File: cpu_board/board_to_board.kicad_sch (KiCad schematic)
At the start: 2 parts

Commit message: grounded
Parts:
- J? (x2): footprint adcs:HIROSE_DF40C-100DP-0.4V(51) -> adcs:DF40C100DP04V51
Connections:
- net GPIO_DISP_B2_00: no longer J?.50
- net GPIO_DISP_B2_01: no longer J?.52
- net GPIO_DISP_B2_02: no longer J?.54
- net GPIO_DISP_B2_03: no longer J?.56
- net GPIO_DISP_B2_04: no longer J?.60
- net GPIO_DISP_B2_05: no longer J?.62
- net GPIO_DISP_B2_06: no longer J?.64
- net GPIO_DISP_B2_07: no longer J?.66
- net GPIO_DISP_B2_08: no longer J?.70
- net GPIO_DISP_B2_09: no longer J?.72
- net GPIO_DISP_B2_10: no longer J?.74
- net GPIO_DISP_B2_11: no longer J?.76
- net GPIO_DISP_B2_12: no longer J?.80
- net GPIO_DISP_B2_13: no longer J?.82
- net GPIO_DISP_B2_14: no longer J?.84
- net GPIO_DISP_B2_15: no longer J?.86
- new net GPIO_EMC_B1_40: J?.50
- new net GPIO_EMC_B1_41: J?.52
- no-connect marks 0 -> 14
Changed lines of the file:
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@@
   (junction (at 99.06 107.95) (diameter 0) (color 0 0 0 0)
   )
+  (no_connect (at 129.54 151.13))
+  (no_connect (at 129.54 166.37))
+  (no_connect (at 129.54 171.45))
+  (no_connect (at 129.54 184.15))
+  (no_connect (at 129.54 186.69))
+  (no_connect (at 129.54 176.53))
+  (no_connect (at 129.54 158.75))
+  (no_connect (at 129.54 153.67))
+  (no_connect (at 129.54 173.99))
+  (no_connect (at 129.54 191.77))
+  (no_connect (at 129.54 189.23))
+  (no_connect (at 129.54 163.83))
+  (no_connect (at 129.54 179.07))
+  (no_connect (at 129.54 161.29))
   (wire (pts (xy 307.975 186.055) (xy 310.515 186.055))
     (stroke (width 0) (type default))
@@
     )
   )
-  (global_label "GPIO_DISP_B2_02" (shape bidirectional) (at 129.54 151.13 0) (fields_autoplaced)
-    (effects (font (size 1.27 1.27)) (justify left))
-    (property "Intersheetrefs" "${INTERSHEET_REFS}" (at 147.3043 151.13 0)
-      (effects (font (size 1.27 1.27)) (justify left) hide)
-    )
-  )
   (global_label "GPIO_AD_10" (shape bidirectional) (at 96.52 148.59 180) (fields_autoplaced)
     (effects (font (size 1.27 1.27)) (justify right))
@@
     )
   )
-  (global_label "GPIO_DISP_B2_12" (shape bidirectional) (at 129.54 184.15 0) (fields_autoplaced)
-    (effects (font (size 1.27 1.27)) (justify left))
-    (property "Intersheetrefs" "${INTERSHEET_REFS}" (at 147.3043 184.15 0)
-      (effects (font (size 1.27 1.27)) (justify left) hide)
-    )
-  )
-  (global_label "GPIO_DISP_B2_15" (shape bidirectional) (at 129.54 191.77 0) (fields_autoplaced)
-    (effects (font (size 1.27 1.27)) (justify left))
-    (property "Intersheetrefs" "${INTERSHEET_REFS}" (at 147.3043 191.77 0)
-      (effects (font (size 1.27 1.27)) (justify left) hide)
-    )
-  )
   (global_label "GPIO_SD_B1_03" (shape bidirectional) (at 129.54 118.11 0) (fields_autoplaced)
     (effects (font (size 1.27 1.27)) (justify left))
@@
     )
   )
+  (global_label "GPIO_EMC_B1_41" (shape input) (at 129.54 148.59 0)
+    (effects (font (size 1.27 1.27)) (justify left))
+    (property "Intersheetrefs" "${INTERSHEET_REFS}" (at 129.54 148.59 0)
+      (effects (font (size 1.27 1.27)) hide)
+    )
+  )
   (global_label "GPIO_EMC_B2_08" (shape bidirectional) (at 278.765 155.575 180)
     (effects (font (size 1.27 1.27)) (justify right))
@@
     )
   )
-  (global_label "GPIO_DISP_B2_00" (shape bidirectional) (at 129.54 146.05 0) (fields_autoplaced)
-    (effects (font (size 1.27 1.27)) (justify left))
-    (property "Intersheetrefs" "${INTERSHEET_REFS}" (at 148.0448 146.05 0)
-      (effects (font (size 1.27 1.27)) (justify left) hide)
-    )
-  )
   (global_label "GPIO_AD_28" (shape bidirectional) (at 96.52 201.93 180) (fields_autoplaced)
     (effects (font (size 1.27 1.27)) (justify right))
@@
     )
   )
-  (global_label "GPIO_DISP_B2_05" (shape bidirectional) (at 129.54 161.29 0) (fields_autoplaced)
-    (effects (font (size 1.27 1.27)) (justify left))
-    (property "Intersheetrefs" "${INTERSHEET_REFS}" (at 147.3043 161.29 0)
-      (effects (font (size 1.27 1.27)) (justify left) hide)
-    )
-  )
   (global_label "GPIO_AD_15" (shape bidirectional) (at 96.52 163.83 180) (fields_autoplaced)
     (effects (font (size 1.27 1.27)) (justify right))
@@
     )
   )
-  (global_label "GPIO_DISP_B2_03" (shape bidirectional) (at 129.54 153.67 0) (fields_autoplaced)
-    (effects (font (size 1.27 1.27)) (justify left))
-    (property "Intersheetrefs" "${INTERSHEET_REFS}" (at 147.3043 153.67 0)
-      (effects (font (size 1.27 1.27)) (justify left) hide)
-    )
-  )
   (global_label "MIPI_CSI_D0_P" (shape input) (at 313.055 188.595 0) (fields_autoplaced)
     (effects (font (size 1.27 1.27)) (justify left))
@@
     )
   )
-  (global_label "GPIO_DISP_B2_09" (shape bidirectional) (at 129.54 173.99 0) (fields_autoplaced)
-    (effects (font (size 1.27 1.27)) (justify left))
-    (property "Intersheetrefs" "${INTERSHEET_REFS}" (at 147.3043 173.99 0)
-      (effects (font (size 1.27 1.27)) (justify left) hide)
-    )
-  )
-  (global_label "GPIO_DISP_B2_08" (shape bidirectional) (at 129.54 171.45 0) (fields_autoplaced)
-    (effects (font (size 1.27 1.27)) (justify left))
-    (property "Intersheetrefs" "${INTERSHEET_REFS}" (at 147.3043 171.45 0)
-      (effects (font (size 1.27 1.27)) (justify left) hide)
-    )
-  )
   (global_label "GPIO_AD_01" (shape bidirectional) (at 96.52 118.11 180) (fields_autoplaced)
     (effects (font (size 1.27 1.27)) (justify right))
@@
     )
   )
-  (global_label "GPIO_DISP_B2_13" (shape bidirectional) (at 129.54 186.69 0) (fields_autoplaced)
-    (effects (font (size 1.27 1.27)) (justify left))
-    (property "Intersheetrefs" "${INTERSHEET_REFS}" (at 147.3043 186.69 0)
-      (effects (font (size 1.27 1.27)) (justify left) hide)
-    )
-  )
-  (global_label "GPIO_DISP_B2_11" (shape bidirectional) (at 129.54 179.07 0) (fields_autoplaced)
-    (effects (font (size 1.27 1.27)) (justify left))
-    (property "Intersheetrefs" "${INTERSHEET_REFS}" (at 147.3043 179.07 0)
-      (effects (font (size 1.27 1.27)) (justify left) hide)
-    )
-  )
   (global_label "USDHC2_DATA2" (shape bidirectional) (at 129.54 130.81 0) (fields_autoplaced)
     (effects (font (size 1.27 1.27)) (justify left))
@@
     )
   )
-  (global_label "GPIO_DISP_B2_06" (shape bidirectional) (at 129.54 163.83 0) (fields_autoplaced)
-    (effects (font (size 1.27 1.27)) (justify left))
-    (property "Intersheetrefs" "${INTERSHEET_REFS}" (at 147.3043 163.83 0)
-      (effects (font (size 1.27 1.27)) (justify left) hide)
+  (global_label "GPIO_EMC_B1_40" (shape output) (at 129.54 146.05 0)
+    (effects (font (size 1.27 1.27)) (justify left))
+    (property "Intersheetrefs" "${INTERSHEET_REFS}" (at 129.54 146.05 0)
+      (effects (font (size 1.27 1.27)) hide)
     )
   )
@@
     )
   )
-  (global_label "GPIO_DISP_B2_10" (shape bidirectional) (at 129.54 176.53 0) (fields_autoplaced)
-    (effects (font (size 1.27 1.27)) (justify left))
-    (property "Intersheetrefs" "${INTERSHEET_REFS}" (at 147.3043 176.53 0)
-      (effects (font (size 1.27 1.27)) (justify left) hide)
-    )
-  )
   (global_label "GPIO_DISP_B2_11" (shape bidirectional) (at 313.055 173.355 0) (fields_autoplaced)
     (effects (font (size 1.27 1.27)) (justify left))
@@
     )
   )
-  (global_label "GPIO_DISP_B2_07" (shape bidirectional) (at 129.54 166.37 0) (fields_autoplaced)
-    (effects (font (size 1.27 1.27)) (justify left))
-    (property "Intersheetrefs" "${INTERSHEET_REFS}" (at 147.3043 166.37 0)
-      (effects (font (size 1.27 1.27)) (justify left) hide)
-    )
-  )
   (global_label "GPIO_LPSR_07" (shape bidirectional) (at 96.52 105.41 180) (fields_autoplaced)
     (effects (font (size 1.27 1.27)) (justify right))
@@
     )
   )
-  (global_label "GPIO_DISP_B2_01" (shape bidirectional) (at 129.54 148.59 0) (fields_autoplaced)
-    (effects (font (size 1.27 1.27)) (justify left))
-    (property "Intersheetrefs" "${INTERSHEET_REFS}" (at 147.3043 148.59 0)
-      (effects (font (size 1.27 1.27)) (justify left) hide)
-    )
-  )
   (global_label "GPIO_DISP_B1_05" (shape bidirectional) (at 313.055 117.475 0) (fields_autoplaced)
     (effects (font (size 1.27 1.27)) (justify left))
@@
     )
   )
-  (global_label "GPIO_DISP_B2_14" (shape bidirectional) (at 129.54 189.23 0) (fields_autoplaced)
-    (effects (font (size 1.27 1.27)) (justify left))
-    (property "Intersheetrefs" "${INTERSHEET_REFS}" (at 147.3043 189.23 0)
-      (effects (font (size 1.27 1.27)) (justify left) hide)
-    )
-  )
   (global_label "GPIO_EMC_B2_00" (shape bidirectional) (at 278.765 132.715 180)
     (effects (font (size 1.27 1.27)) (justify right))
@@
     (effects (font (size 1.27 1.27)) (justify left))
     (property "Intersheetrefs" "${INTERSHEET_REFS}" (at 148.3926 120.65 0)
-      (effects (font (size 1.27 1.27)) (justify left) hide)
-    )
-  )
-  (global_label "GPIO_DISP_B2_04" (shape bidirectional) (at 129.54 158.75 0) (fields_autoplaced)
-    (effects (font (size 1.27 1.27)) (justify left))
-    (property "Intersheetrefs" "${INTERSHEET_REFS}" (at 147.3043 158.75 0)
       (effects (font (size 1.27 1.27)) (justify left) hide)
     )
@@
       (effects (font (size 1.27 1.27)) hide)
     )
-    (property "Footprint" "adcs:HIROSE_DF40C-100DP-0.4V(51)" (at 106.68 80.01 0)
+    (property "Footprint" "adcs:DF40C100DP04V51" (at 106.68 80.01 0)
       (effects (font (size 1.27 1.27)) hide)
     )
@@
     (property "Footprint (for JLCPCB)" "" (at 106.68 80.01 0)
       (effects (font (size 1.27 1.27)) hide)
+    )
+    (property "DigiKey Part Number" "" (at 106.68 80.01 0)
+      (effects (font (size 1.27 1.27)) hide)
+    )
+    (property "Tolerance" "" (at 106.68 80.01 0)
+      (effects (font (size 1.27 1.27)))
+    )
+    (property "Power Rating" "" (at 106.68 80.01 0)
+      (effects (font (size 1.27 1.27)))
     )
     (pin "1")
@@
       (effects (font (size 1.27 1.27)) hide)
     )
-    (property "Footprint" "adcs:HIROSE_DF40C-100DP-0.4V(51)" (at 290.195 76.835 0)
+    (property "Footprint" "adcs:DF40C100DP04V51" (at 290.195 76.835 0)
       (effects (font (size 1.27 1.27)) hide)
     )
@@
       (effects (font (size 1.27 1.27)) hide)
     )
+    (property "DigiKey Part Number" "" (at 290.195 76.835 0)
+      (effects (font (size 1.27 1.27)) hide)
+    )
+    (property "Tolerance" "" (at 290.195 76.835 0)
+      (effects (font (size 1.27 1.27)))
+    )
+    (property "Power Rating" "" (at 290.195 76.835 0)
+      (effects (font (size 1.27 1.27)))
+    )
     (pin "1")

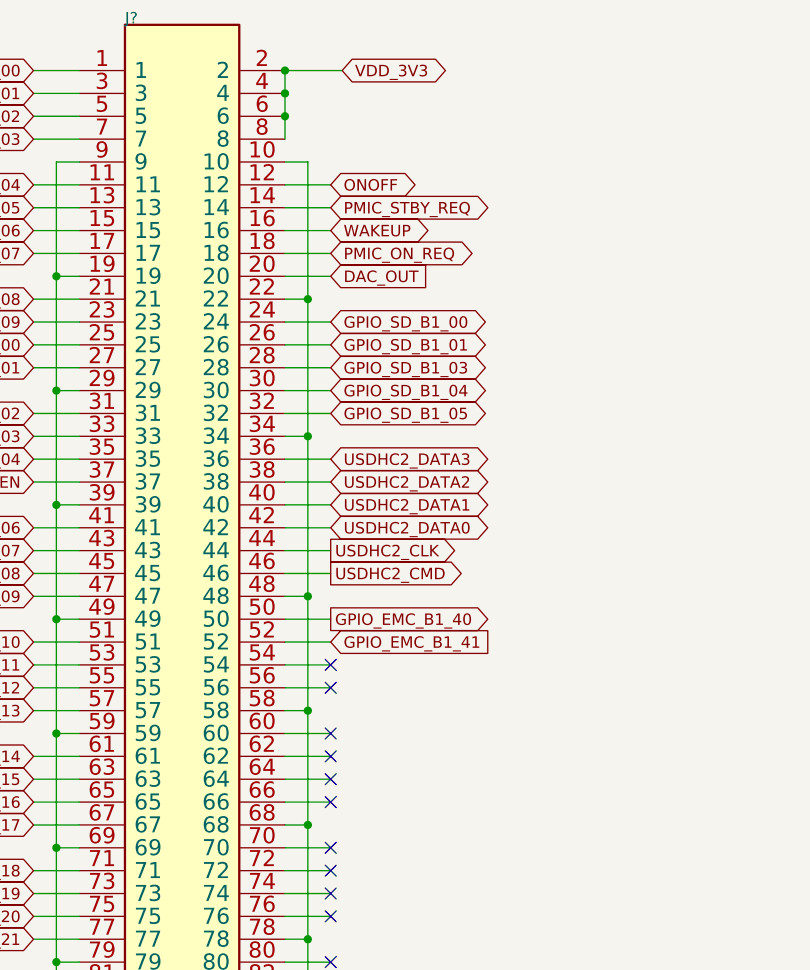
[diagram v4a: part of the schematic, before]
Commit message: add load switch
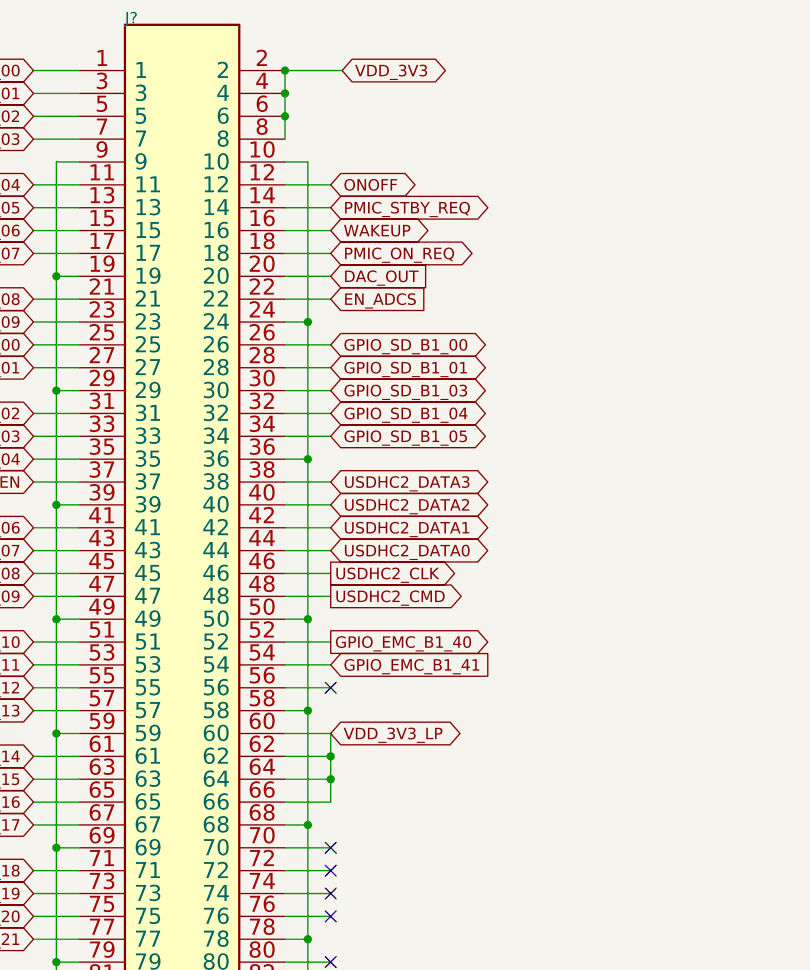
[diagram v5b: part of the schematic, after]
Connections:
- net GND: now also J?.24, J?.36, J?.50; no longer J?.22, J?.34, J?.48
- net GPIO_EMC_B1_40: now also J?.52; no longer J?.50
- net GPIO_EMC_B1_41: now also J?.54; no longer J?.52
- net GPIO_SD_B1_00: now also J?.26; no longer J?.24
- net GPIO_SD_B1_01: now also J?.28; no longer J?.26
- net GPIO_SD_B1_03: now also J?.30; no longer J?.28
- net GPIO_SD_B1_04: now also J?.32; no longer J?.30
- net GPIO_SD_B1_05: now also J?.34; no longer J?.32
- net USDHC2_CLK: now also J?.46; no longer J?.44
- net USDHC2_CMD: now also J?.48; no longer J?.46
- net USDHC2_DATA0: now also J?.44; no longer J?.42
- net USDHC2_DATA1: now also J?.42; no longer J?.40
- net USDHC2_DATA2: now also J?.40; no longer J?.38
- net USDHC2_DATA3: now also J?.38; no longer J?.36
- net VDD_3V3_LP: now reaches J?.60
- net VDD_3V3_LP: now also J?.62, J?.64, J?.66
- new net EN_ADCS: J?.22
- no-connect marks 14 -> 9

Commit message: pre-autorouter
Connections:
- net MIPI_CSI_CK_N: no longer names the net of J?.94
- net MIPI_CSI_CK_P: no longer names the net of J?.92
- net MIPI_CSI_D0_N: no longer names the net of J?.88
- net MIPI_CSI_D0_P: no longer names the net of J?.86
- net MIPI_CSI_D1_N: no longer names the net of J?.100
- net MIPI_CSI_D1_P: no longer names the net of J?.98
- no-connect marks 9 -> 15
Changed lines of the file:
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@@
   )
   (no_connect (at 129.54 171.45))
+  (no_connect (at 313.055 206.375))
   (no_connect (at 129.54 184.15))
   (no_connect (at 129.54 186.69))
+  (no_connect (at 313.055 196.215))
   (no_connect (at 129.54 176.53))
   (no_connect (at 129.54 153.67))
   (no_connect (at 129.54 173.99))
+  (no_connect (at 313.055 198.755))
+  (no_connect (at 313.055 203.835))
   (no_connect (at 129.54 191.77))
+  (no_connect (at 313.055 188.595))
   (no_connect (at 129.54 189.23))
+  (no_connect (at 313.055 191.135))
   (no_connect (at 129.54 179.07))
   (wire (pts (xy 307.975 186.055) (xy 310.515 186.055))
@@
     )
   )
-  (global_label "MIPI_CSI_D0_N" (shape input) (at 313.055 191.135 0) (fields_autoplaced)
-    (effects (font (size 1.27 1.27)) (justify left))
-    (property "Intersheetrefs" "${INTERSHEET_REFS}" (at 329.0995 191.135 0)
-      (effects (font (size 1.27 1.27)) (justify left) hide)
-    )
-  )
-  (global_label "MIPI_CSI_D0_P" (shape input) (at 313.055 188.595 0) (fields_autoplaced)
-    (effects (font (size 1.27 1.27)) (justify left))
-    (property "Intersheetrefs" "${INTERSHEET_REFS}" (at 329.0414 188.595 0)
-      (effects (font (size 1.27 1.27)) (justify left) hide)
-    )
-  )
   (global_label "GPIO_EMC_B2_12" (shape bidirectional) (at 278.765 168.275 180)
     (effects (font (size 1.27 1.27)) (justify right))
@@
     )
   )
-  (global_label "MIPI_CSI_CK_P" (shape input) (at 313.055 196.215 0) (fields_autoplaced)
-    (effects (font (size 1.27 1.27)) (justify left))
-    (property "Intersheetrefs" "${INTERSHEET_REFS}" (at 329.0995 196.215 0)
-      (effects (font (size 1.27 1.27)) (justify left) hide)
-    )
-  )
   (global_label "GPIO_DISP_B2_12" (shape bidirectional) (at 313.055 175.895 0) (fields_autoplaced)
     (effects (font (size 1.27 1.27)) (justify left))
@@
     )
   )
-  (global_label "MIPI_CSI_CK_N" (shape input) (at 313.055 198.755 0) (fields_autoplaced)
-    (effects (font (size 1.27 1.27)) (justify left))
-    (property "Intersheetrefs" "${INTERSHEET_REFS}" (at 329.1576 198.755 0)
-      (effects (font (size 1.27 1.27)) (justify left) hide)
-    )
-  )
   (global_label "GPIO_AD_33" (shape bidirectional) (at 129.54 201.93 0) (fields_autoplaced)
     (effects (font (size 1.27 1.27)) (justify left))
@@
     )
   )
-  (global_label "MIPI_CSI_D1_P" (shape input) (at 313.055 203.835 0) (fields_autoplaced)
-    (effects (font (size 1.27 1.27)) (justify left))
-    (property "Intersheetrefs" "${INTERSHEET_REFS}" (at 329.0414 203.835 0)
-      (effects (font (size 1.27 1.27)) (justify left) hide)
-    )
-  )
   (global_label "GPIO_SNVS_09" (shape input) (at 278.765 127.635 180) (fields_autoplaced)
     (effects (font (size 1.27 1.27)) (justify right))
@@
     )
   )
-  (global_label "MIPI_CSI_D1_N" (shape input) (at 313.055 206.375 0) (fields_autoplaced)
-    (effects (font (size 1.27 1.27)) (justify left))
-    (property "Intersheetrefs" "${INTERSHEET_REFS}" (at 329.0995 206.375 0)
-      (effects (font (size 1.27 1.27)) (justify left) hide)
-    )
-  )
